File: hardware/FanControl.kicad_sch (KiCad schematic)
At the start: 2 parts, among them IC9 TPL7407LADR

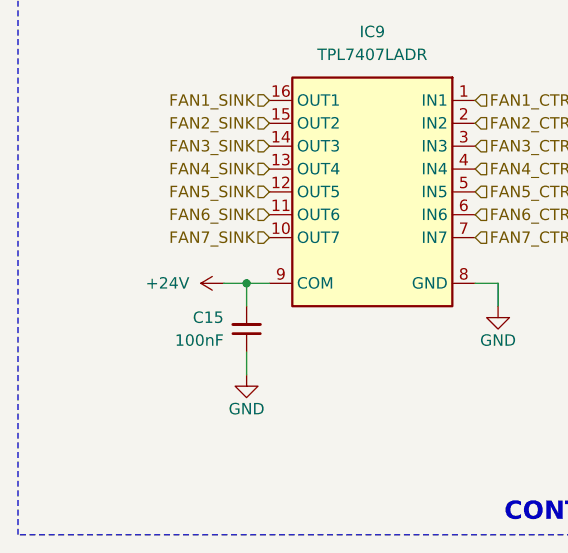
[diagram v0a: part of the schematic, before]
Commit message: mcu pinout done
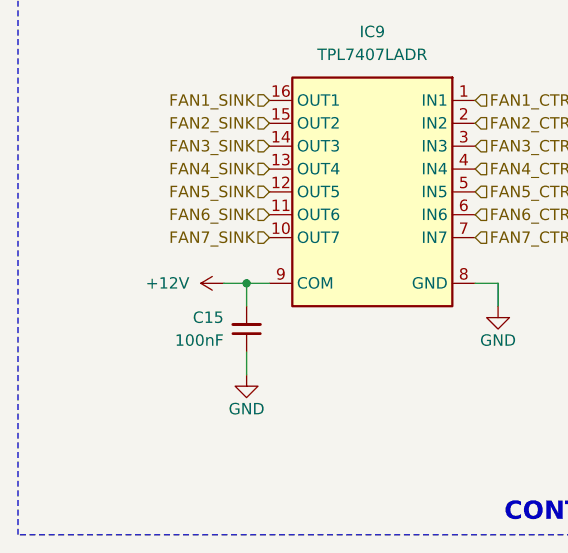
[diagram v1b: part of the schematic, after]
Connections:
- net +24V renamed +12V
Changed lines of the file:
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@@
 			)
 		)
-		(property "Value" "+24V"
+		(property "Value" "+12V"
 			(at 125.73 110.49 90)
 			(effects

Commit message: mama comit
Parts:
- removed C15: 100nF, Capacitor_SMD:C_0603_1608Metric, symbol Device:C_Small
- removed IC9: TPL7407LADR, Package_SO:SOIC-16_3.9x9.9mm_P1.27mm, symbol Samacsys_kicad_sym:TPL7407LADR

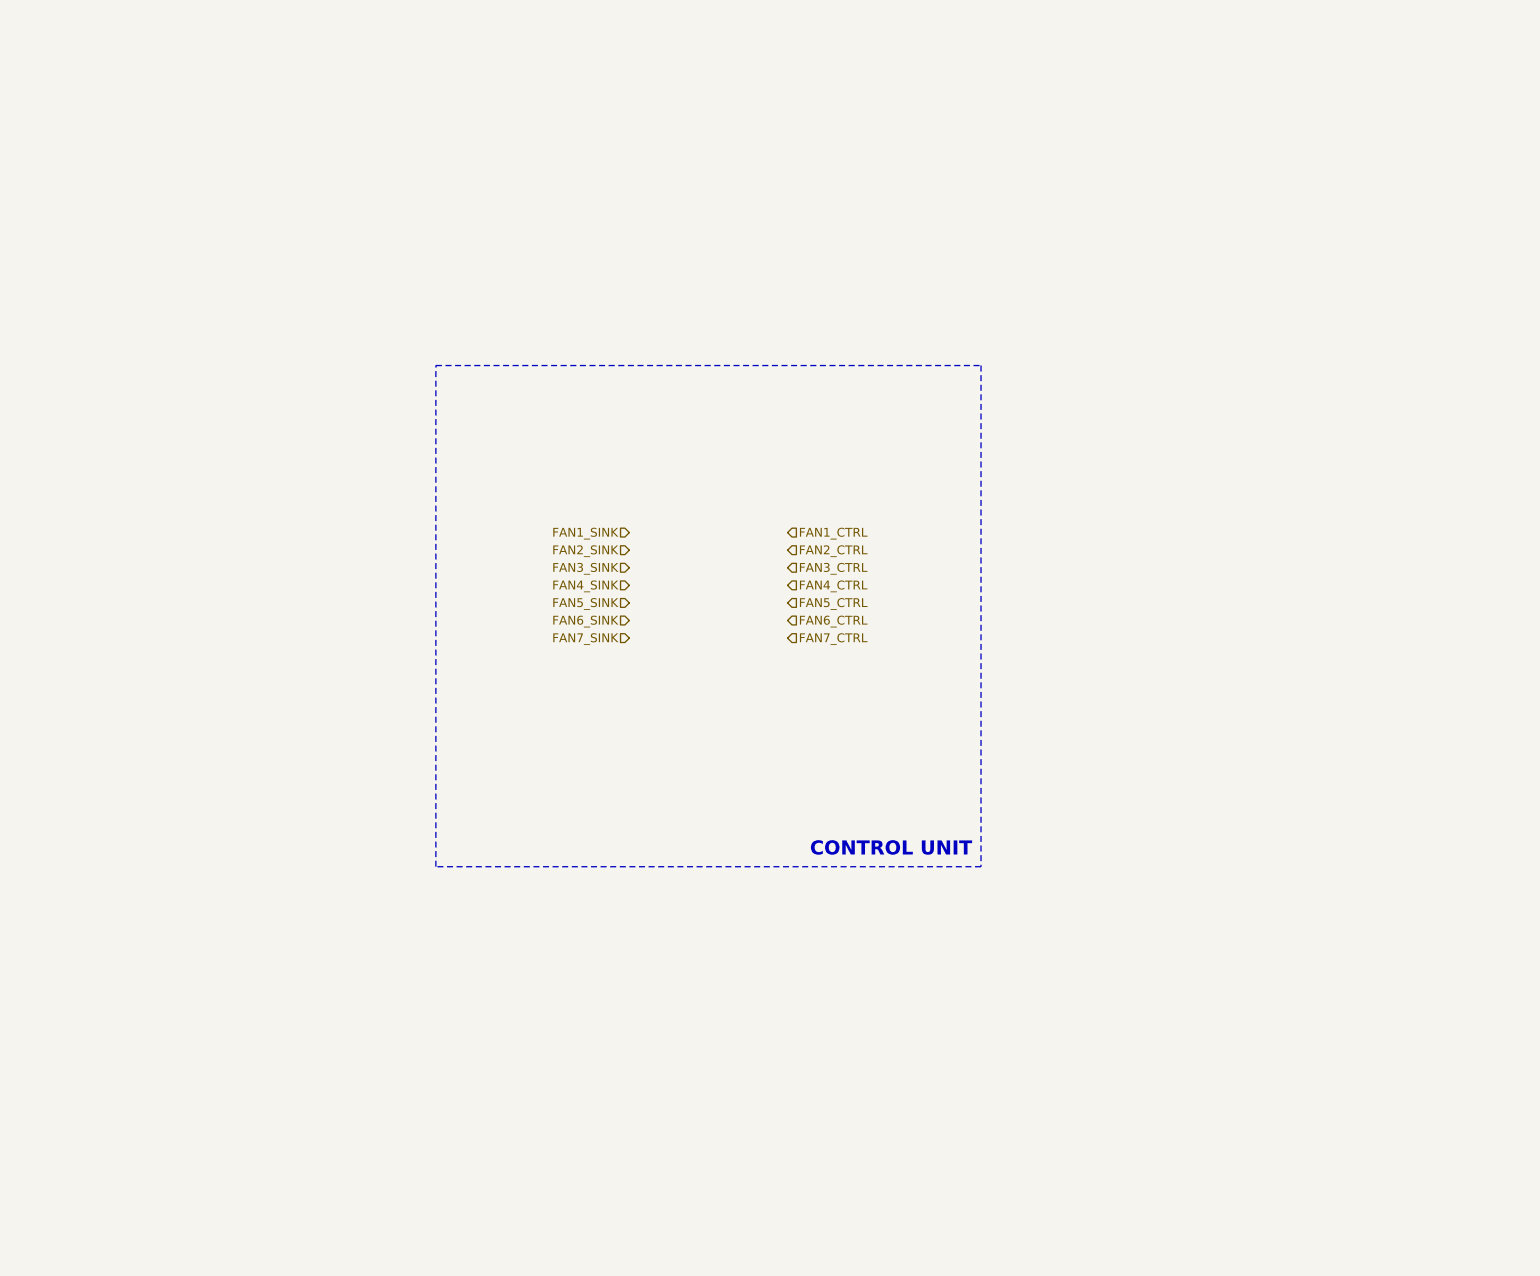
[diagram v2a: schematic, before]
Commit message: all but the communications sections done
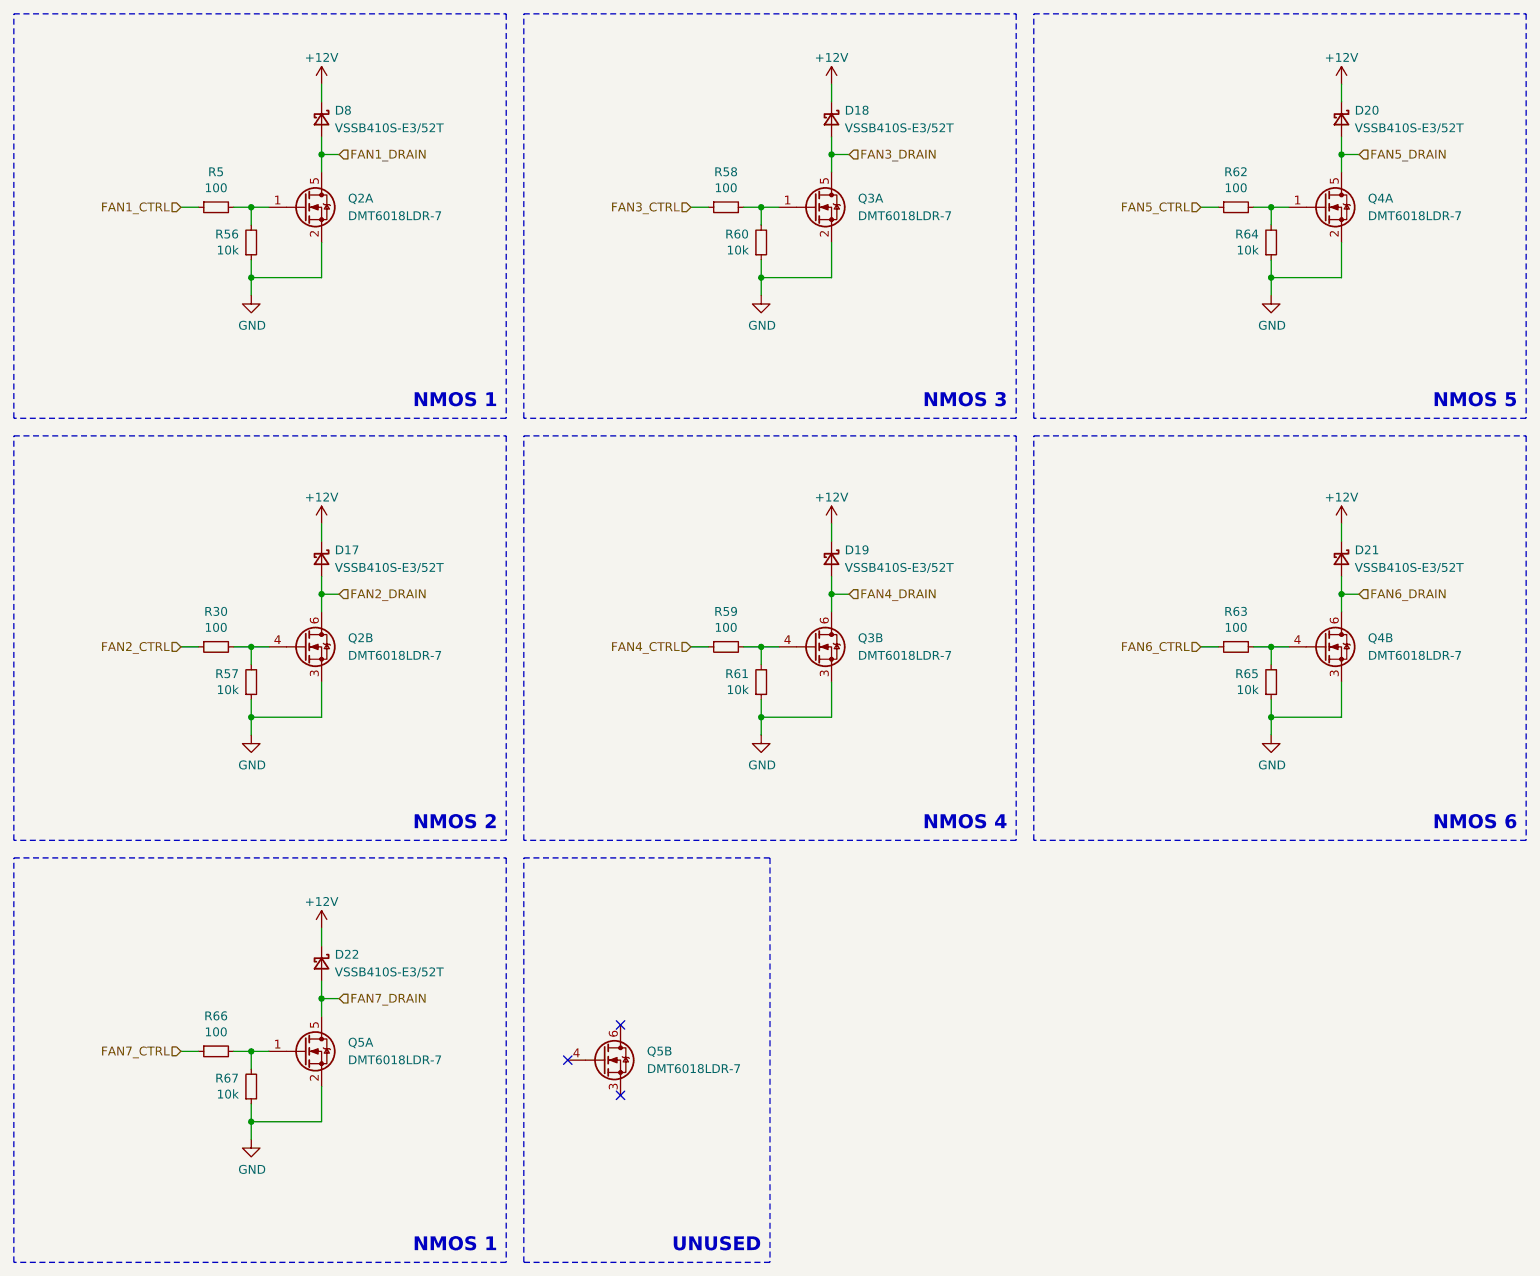
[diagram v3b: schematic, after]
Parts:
- added D17, D18, D19, D20, D21, D22, D8: VSSB410S-E3/52T, Diode_SMD:D_SOD-123, symbol Device:D_Schottky_Small
- added Q2, Q3, Q4, Q5: DMT6018LDR-7, Samacsys:DMT6018LDR7, symbol Samacsys_kicad_sym:DMT6018LDR-7
- added R30, R5, R58, R59, R62, R63, R66: 100, Resistor_SMD:R_0603_1608Metric, symbol Device:R_Small
- added R56, R57, R60, R61, R64, R65, R67: 10k, Resistor_SMD:R_0603_1608Metric, symbol Device:R_Small
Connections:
- net FAN1_CTRL: now also R5.1
- net FAN2_CTRL: now also R30.1
- net FAN3_CTRL: now also R58.1
- net FAN4_CTRL: now also R59.1
- net FAN5_CTRL: now also R62.1
- net FAN6_CTRL: now also R63.1
- net FAN7_CTRL: now also R66.1
- new net: Q3.4 (G2), R59.2, R61.2
- new net: Q2.1 (G1), R5.2, R56.2
- new net: Q4.1 (G1), R62.2, R64.2
- new net: Q4.4 (G2), R63.2, R65.2
- new net: Q2.4 (G2), R30.2, R57.2
- new net: Q5.1 (G1), R66.2, R67.2
- new net: Q3.1 (G1), R58.2, R60.2
- new net +12V: D17.1 (K), D18.1 (K), D19.1 (K), D20.1 (K), D21.1 (K), D22.1 (K), D8.1 (K)
- new net FAN1_DRAIN: D8.2 (A), Q2.5 (D1)
- new net FAN2_DRAIN: D17.2 (A), Q2.6 (D2)
- new net FAN3_DRAIN: D18.2 (A), Q3.5 (D1)
- new net FAN4_DRAIN: D19.2 (A), Q3.6 (D2)
- new net FAN5_DRAIN: D20.2 (A), Q4.5 (D1)
- new net FAN6_DRAIN: D21.2 (A), Q4.6 (D2)
- new net FAN7_DRAIN: D22.2 (A), Q5.5 (D1)
- new net GND: Q2.2 (S1), Q2.3 (S2), Q3.2 (S1), Q3.3 (S2), Q4.2 (S1), Q4.3 (S2), Q5.2 (S1), R56.1, R57.1, R60.1, R61.1, R64.1, R65.1, R67.1
- no-connect marks 0 -> 3
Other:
- note added: "NMOS 1"
- note added: "NMOS 2"
- note added: "NMOS 3"
- note added: "NMOS 4"
- note added: "NMOS 5"
- note added: "NMOS 6"
- note added: "UNUSED"
- note removed: "CONTROL UNIT"

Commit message: sync
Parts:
- R56, R57, R60, R61, R64, R65, R67: Mouser Price/Stock (none) -> https://www.mouser.pl/ProductDetail/YAGEO/RT0603DRE07100KL?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

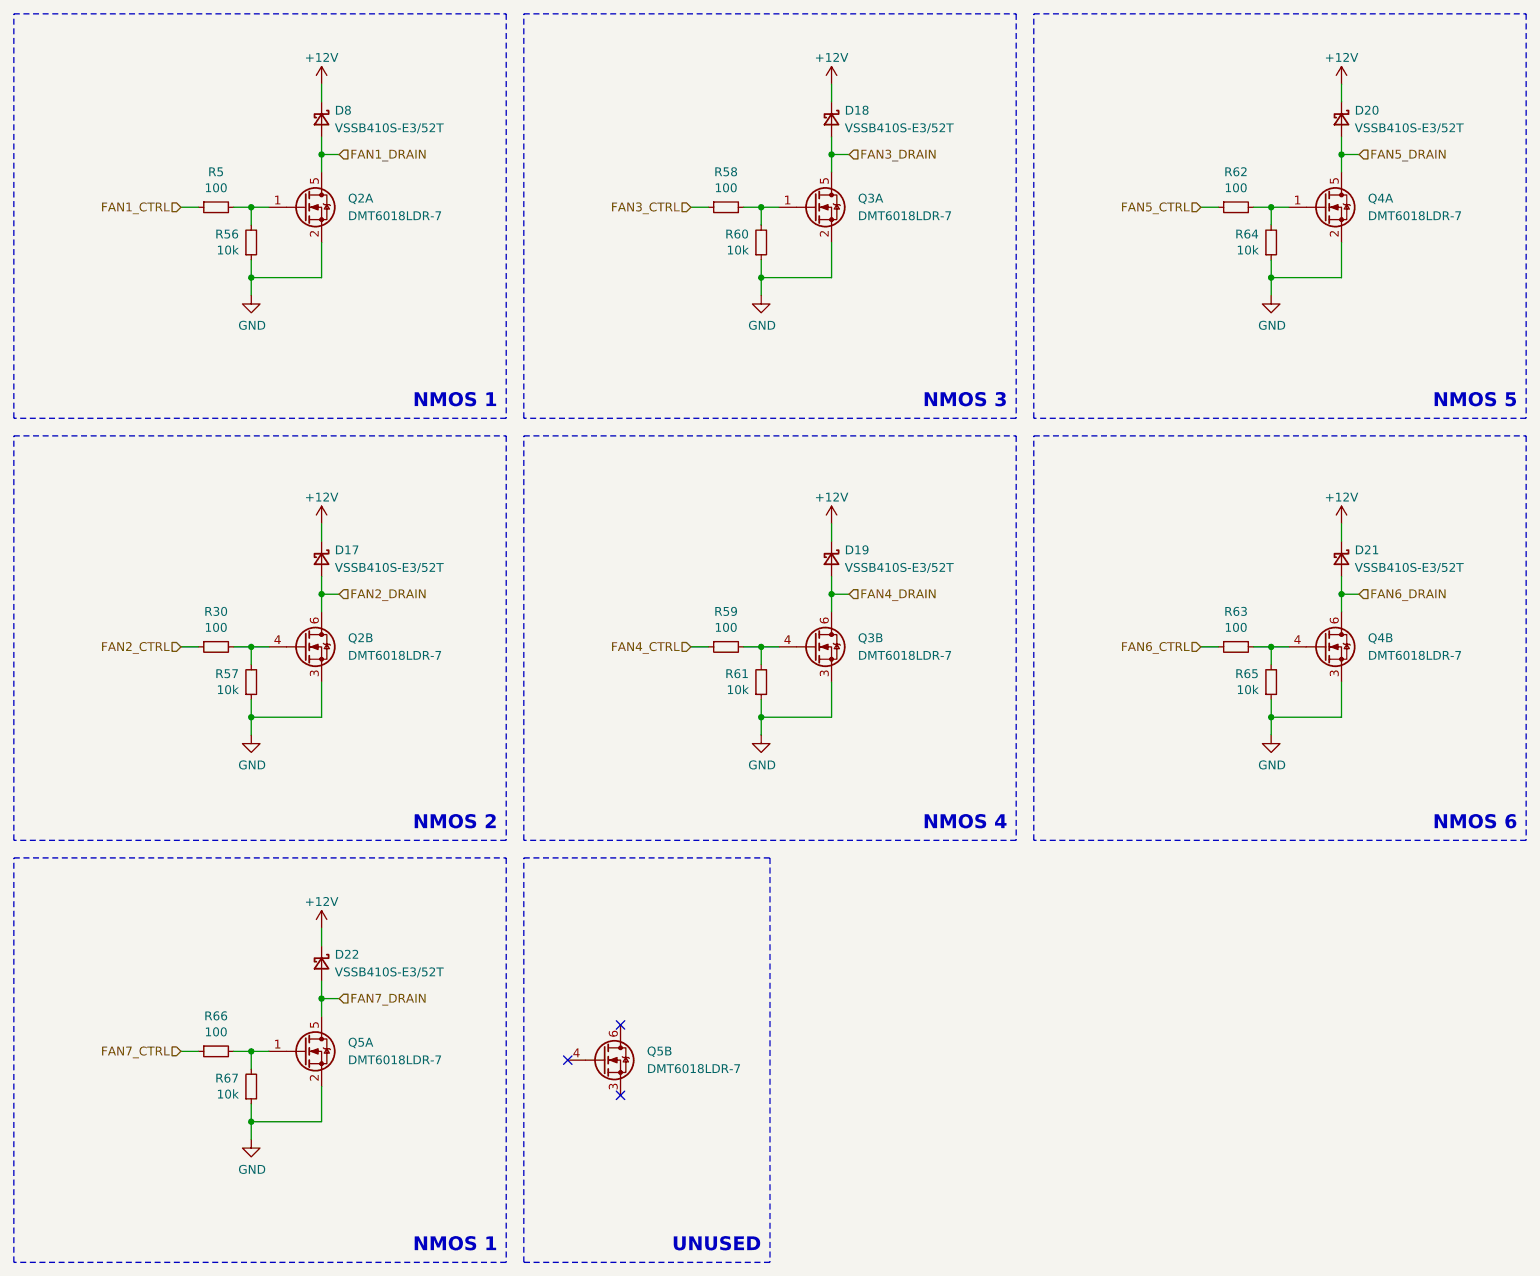
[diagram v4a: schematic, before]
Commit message: LV section component placement done
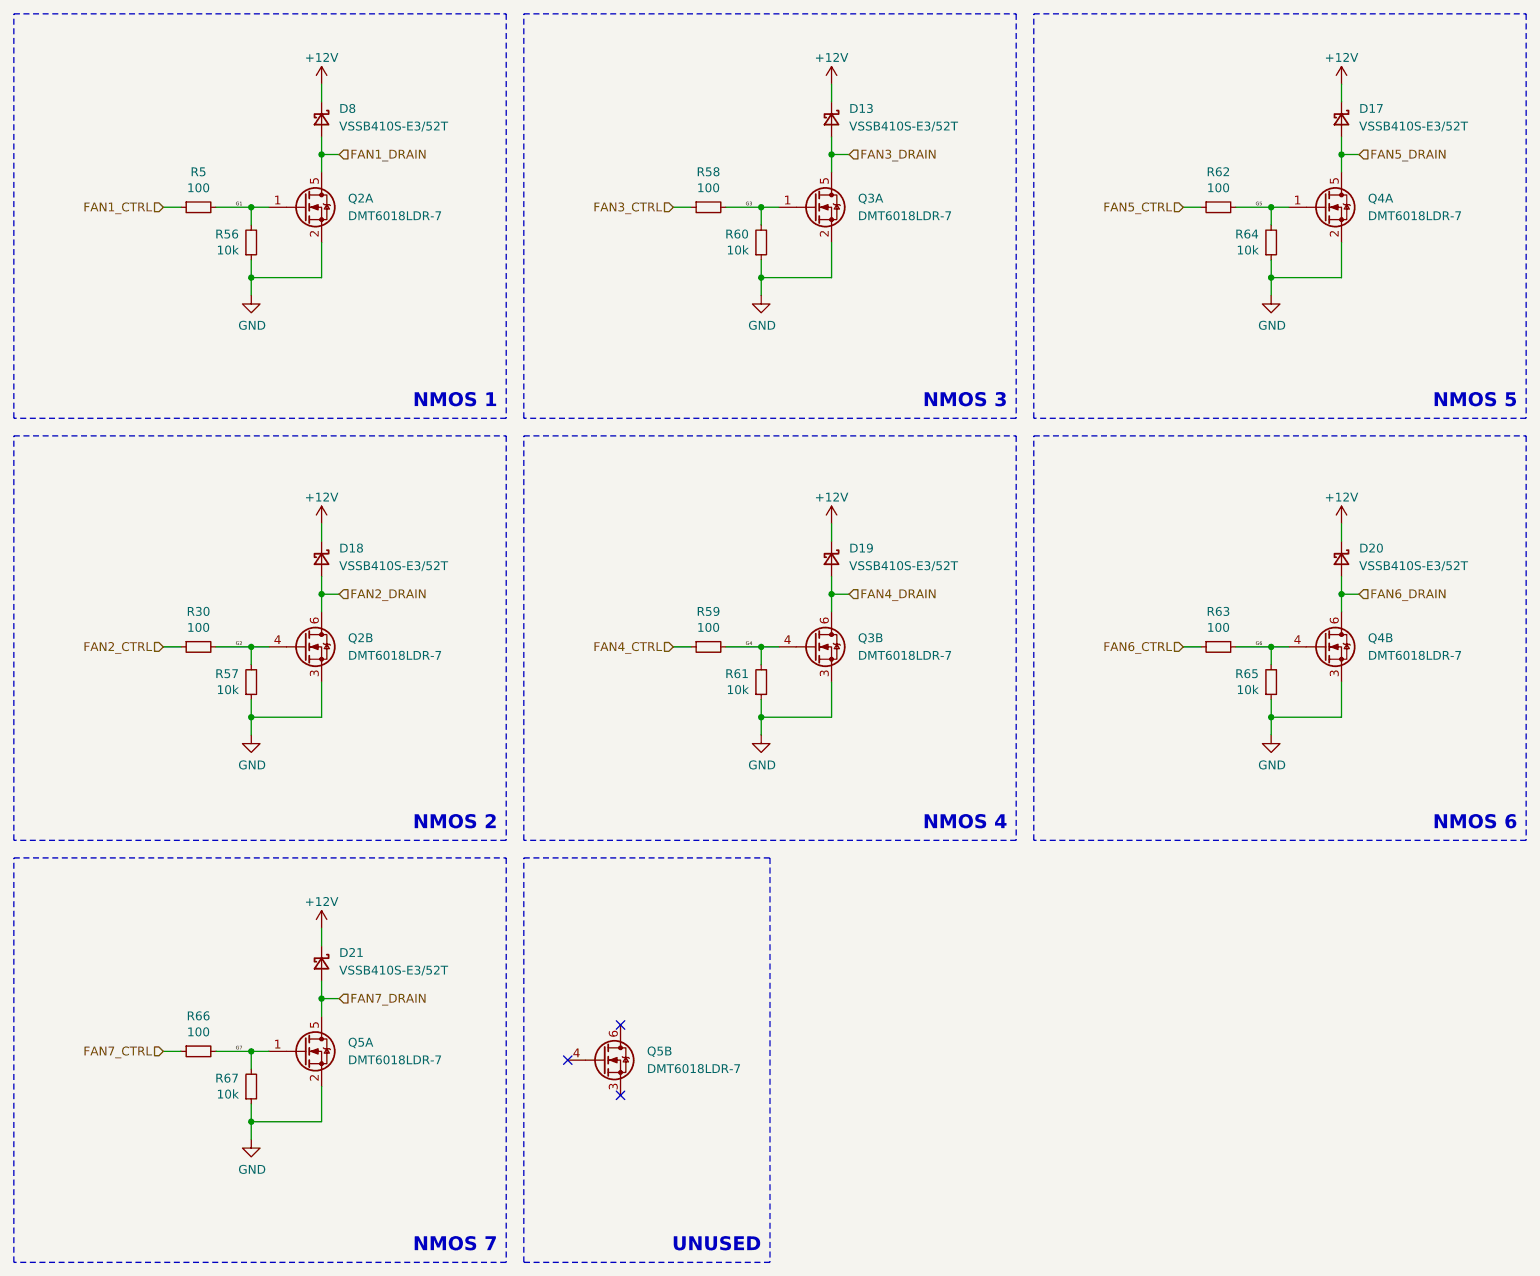
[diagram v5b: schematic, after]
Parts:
- removed D22: VSSB410S-E3/52T, Diode_SMD:D_SOD-123, symbol Device:D_Schottky_Small
- added D13: VSSB410S-E3/52T, Diode_SMD:D_SOD-123, symbol Device:D_Schottky_Small
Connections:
- net +12V: now also D13.1 (K)
- net FAN2_DRAIN: now also D18.2 (A); no longer D17.2 (A)
- net FAN3_DRAIN: now also D13.2 (A); no longer D18.2 (A)
- net FAN5_DRAIN: now also D17.2 (A); no longer D20.2 (A)
- net FAN6_DRAIN: now also D20.2 (A); no longer D21.2 (A)
- net FAN7_DRAIN: now also D21.2 (A)
- net G4: now reaches Q3.4 (G2), R59.2, R61.2
- net G1: now reaches Q2.1 (G1), R5.2, R56.2
- net G5: now reaches Q4.1 (G1), R62.2, R64.2
- net G6: now reaches Q4.4 (G2), R63.2, R65.2
- net G2: now reaches Q2.4 (G2), R30.2, R57.2
- net G7: now reaches Q5.1 (G1), R66.2, R67.2
- net G3: now reaches Q3.1 (G1), R58.2, R60.2
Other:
- note added: "NMOS 7"
- moved on the sheet: R30, R5, R58, R59, R62, R63, R66
